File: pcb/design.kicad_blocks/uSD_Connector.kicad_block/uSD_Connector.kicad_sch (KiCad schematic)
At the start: 10 parts, among them J3 Micro_SD_Card

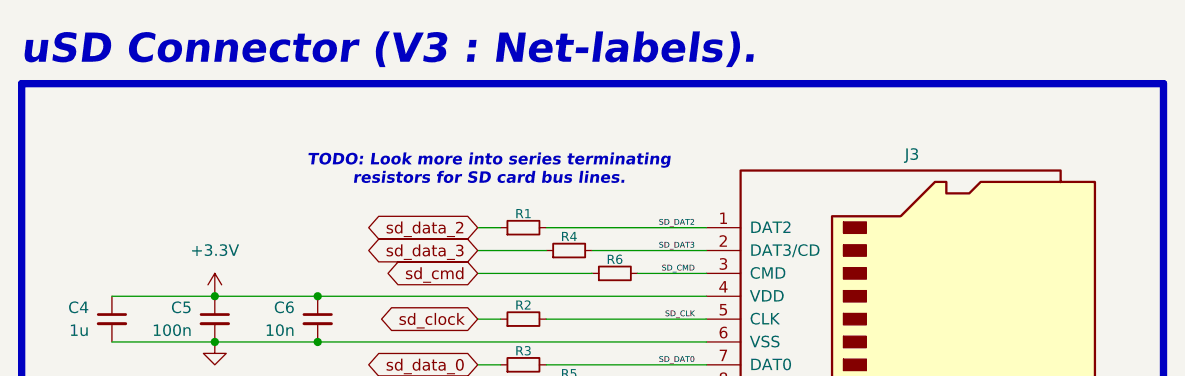
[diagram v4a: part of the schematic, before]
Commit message: Added part number to uSD connector.
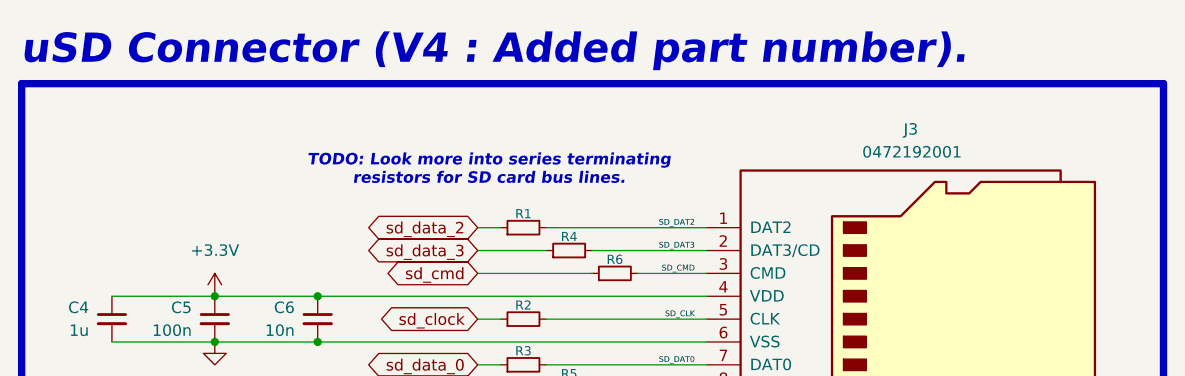
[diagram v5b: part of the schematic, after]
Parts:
- J3: value Micro_SD_Card -> 0472192001
- R1, R2, R3, R4, R5, R6: now in the parts list
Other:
- note added: "uSD Connector (V4 : Added part number)."
- note removed: "uSD Connector (V3 : Net-labels)."
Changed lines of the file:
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@@
 		)
 	)
-	(text "uSD Connector (V3 : Net-labels)."
+	(text "uSD Connector (V4 : Added part number)."
 		(exclude_from_sim no)
 		(at 340.36 165.1 0)
@@
 		(unit 1)
 		(exclude_from_sim no)
-		(in_bom no)
+		(in_bom yes)
 		(on_board yes)
 		(dnp no)
@@
 		(unit 1)
 		(exclude_from_sim no)
-		(in_bom no)
+		(in_bom yes)
 		(on_board yes)
 		(dnp no)
@@
 		(unit 1)
 		(exclude_from_sim no)
-		(in_bom no)
+		(in_bom yes)
 		(on_board yes)
 		(dnp no)
@@
 		(unit 1)
 		(exclude_from_sim no)
-		(in_bom no)
+		(in_bom yes)
 		(on_board yes)
 		(dnp no)
@@
 		(unit 1)
 		(exclude_from_sim no)
-		(in_bom no)
+		(in_bom yes)
 		(on_board yes)
 		(dnp no)
@@
 		(dnp no)
 		(property "Reference" "J3"
-			(at 439.42 174.752 0)
-			(effects
-				(font
-					(size 1.27 1.27)
-				)
-			)
-		)
-		(property "Value" "Micro_SD_Card"
-			(at 440.055 173.99 0)
-			(effects
-				(font
-					(size 1.27 1.27)
-				)
-				(hide yes)
+			(at 439.293 171.958 0)
+			(effects
+				(font
+					(size 1.27 1.27)
+				)
+			)
+		)
+		(property "Value" "0472192001"
+			(at 439.42 174.498 0)
+			(effects
+				(font
+					(size 1.27 1.27)
+				)
 			)
 		)
@@
 		(unit 1)
 		(exclude_from_sim no)
-		(in_bom no)
+		(in_bom yes)
 		(on_board yes)
 		(dnp no)

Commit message: Addressed ERC issues.
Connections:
- net SD_CLK renamed SD_CONNECTOR_CLK
- net SD_CMD renamed SD_CONNECTOR_CMD
- net SD_DAT0 renamed SD_CONNECTOR_DAT0
- net SD_DAT1 renamed SD_CONNECTOR_DAT1
- net SD_DAT2 renamed SD_CONNECTOR_DAT2
- net SD_DAT3 renamed SD_CONNECTOR_DAT3
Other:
- note added: "uSD Connector (V5 : Addressed ERC)."
- note removed: "uSD Connector (V4 : Added part number)."
- moved on the sheet: J3
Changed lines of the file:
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@@
 	(rectangle
 		(start 340.487 166.878)
-		(end 467.36 212.09)
+		(end 477.52 212.09)
 		(stroke
 			(width 0.8128)
@@
 		)
 	)
-	(text "uSD Connector (V4 : Added part number)."
+	(text "uSD Connector (V5 : Addressed ERC)."
 		(exclude_from_sim no)
 		(at 340.36 165.1 0)
@@
 	(wire
 		(pts
-			(xy 398.78 182.88) (xy 416.56 182.88)
-		)
-		(stroke
-			(width 0)
-			(type default)
-		)
-	)
-	(wire
-		(pts
-			(xy 403.86 200.66) (xy 416.56 200.66)
-		)
-		(stroke
-			(width 0)
-			(type default)
-		)
-	)
-	(wire
-		(pts
-			(xy 373.38 195.58) (xy 416.56 195.58)
-		)
-		(stroke
-			(width 0)
-			(type default)
-		)
-	)
-	(wire
-		(pts
 			(xy 361.95 195.58) (xy 350.52 195.58)
 		)
@@
 	(wire
 		(pts
-			(xy 403.86 185.42) (xy 416.56 185.42)
-		)
-		(stroke
-			(width 0)
-			(type default)
-		)
-	)
-	(wire
-		(pts
-			(xy 398.78 198.12) (xy 416.56 198.12)
+			(xy 373.38 190.5) (xy 425.45 190.5)
+		)
+		(stroke
+			(width 0)
+			(type default)
+		)
+	)
+	(wire
+		(pts
+			(xy 403.86 185.42) (xy 425.45 185.42)
 		)
 		(stroke
@@
 	(wire
 		(pts
+			(xy 408.94 187.96) (xy 425.45 187.96)
+		)
+		(stroke
+			(width 0)
+			(type default)
+		)
+	)
+	(wire
+		(pts
 			(xy 361.95 190.5) (xy 373.38 190.5)
 		)
@@
 	(wire
 		(pts
+			(xy 398.78 193.04) (xy 425.45 193.04)
+		)
+		(stroke
+			(width 0)
+			(type default)
+		)
+	)
+	(wire
+		(pts
+			(xy 403.86 200.66) (xy 425.45 200.66)
+		)
+		(stroke
+			(width 0)
+			(type default)
+		)
+	)
+	(wire
+		(pts
 			(xy 393.7 182.88) (xy 391.16 182.88)
 		)
@@
 	(wire
 		(pts
+			(xy 398.78 198.12) (xy 425.45 198.12)
+		)
+		(stroke
+			(width 0)
+			(type default)
+		)
+	)
+	(wire
+		(pts
+			(xy 373.38 195.58) (xy 425.45 195.58)
+		)
+		(stroke
+			(width 0)
+			(type default)
+		)
+	)
+	(wire
+		(pts
 			(xy 350.52 190.5) (xy 361.95 190.5)
 		)
@@
 	(wire
 		(pts
-			(xy 373.38 190.5) (xy 416.56 190.5)
-		)
-		(stroke
-			(width 0)
-			(type default)
-		)
-	)
-	(wire
-		(pts
-			(xy 398.78 193.04) (xy 416.56 193.04)
+			(xy 398.78 182.88) (xy 425.45 182.88)
 		)
 		(stroke
@@
 		)
 	)
-	(wire
-		(pts
-			(xy 408.94 187.96) (xy 416.56 187.96)
-		)
-		(stroke
-			(width 0)
-			(type default)
-		)
-	)
-	(label "SD_CMD"
-		(at 415.29 187.96 180)
+	(label "SD_CONNECTOR_CMD"
+		(at 424.18 187.96 180)
 		(effects
 			(font
@@
 		)
 	)
-	(label "SD_CLK"
-		(at 415.29 193.04 180)
+	(label "SD_CONNECTOR_CLK"
+		(at 424.18 193.04 180)
 		(effects
 			(font
@@
 		)
 	)
-	(label "SD_DAT0"
-		(at 415.29 198.12 180)
+	(label "SD_CONNECTOR_DAT0"
+		(at 424.18 198.12 180)
 		(effects
 			(font
@@
 		)
 	)
-	(label "SD_DAT3"
-		(at 415.29 185.42 180)
+	(label "SD_CONNECTOR_DAT3"
+		(at 424.18 185.42 180)
 		(effects
 			(font
@@
 		)
 	)
-	(label "SD_DAT2"
-		(at 415.29 182.88 180)
+	(label "SD_CONNECTOR_DAT2"
+		(at 424.18 182.88 180)
 		(effects
 			(font
@@
 		)
 	)
-	(label "SD_DAT1"
-		(at 415.29 200.66 180)
+	(label "SD_CONNECTOR_DAT1"
+		(at 424.18 200.66 180)
 		(effects
 			(font
@@
 	(symbol
 		(lib_id "Connector:Micro_SD_Card")
-		(at 439.42 190.5 0)
+		(at 448.31 190.5 0)
 		(unit 1)
 		(exclude_from_sim no)
@@
 		(dnp no)
 		(property "Reference" "J3"
-			(at 439.293 171.958 0)
+			(at 448.183 171.958 0)
 			(effects
 				(font
@@
 		)
 		(property "Value" "0472192001"
-			(at 439.42 174.498 0)
+			(at 448.31 174.498 0)
 			(effects
 				(font
@@
 		)
 		(property "Footprint" "pcb:microSD_HC_Molex_47219-2001"
-			(at 468.63 182.88 0)
+			(at 477.52 182.88 0)
 			(effects
 				(font
@@
 		)
 		(property "Datasheet" "https://www.we-online.com/components/products/datasheet/693072010801.pdf"
-			(at 439.42 190.5 0)
+			(at 448.31 190.5 0)
 			(effects
 				(font
@@
 		)
 		(property "Description" "Micro SD Card Socket"
-			(at 439.42 190.5 0)
+			(at 448.31 190.5 0)
 			(effects
 				(font
@@
 	(symbol
 		(lib_id "power:GND")
-		(at 459.74 205.74 90)
+		(at 468.63 205.74 90)
 		(unit 1)
 		(exclude_from_sim no)
@@
 		(fields_autoplaced yes)
 		(property "Reference" "#PWR026"
-			(at 466.09 205.74 0)
+			(at 474.98 205.74 0)
 			(effects
 				(font
@@
 		)
 		(property "Value" "GND"
-			(at 463.55 205.7399 90)
+			(at 472.44 205.7399 90)
 			(effects
 				(font
@@
 		)
 		(property "Footprint" ""
-			(at 459.74 205.74 0)
+			(at 468.63 205.74 0)
 			(effects
 				(font
@@
 		)
 		(property "Datasheet" ""
-			(at 459.74 205.74 0)
+			(at 468.63 205.74 0)
 			(effects
 				(font
@@
 		)
 		(property "Description" "Power symbol creates a global label with name \"GND\" , ground"
-			(at 459.74 205.74 0)
-			(effects
-				(font
+			(at 468.63 205.74 0)
+			(effects
+				(font

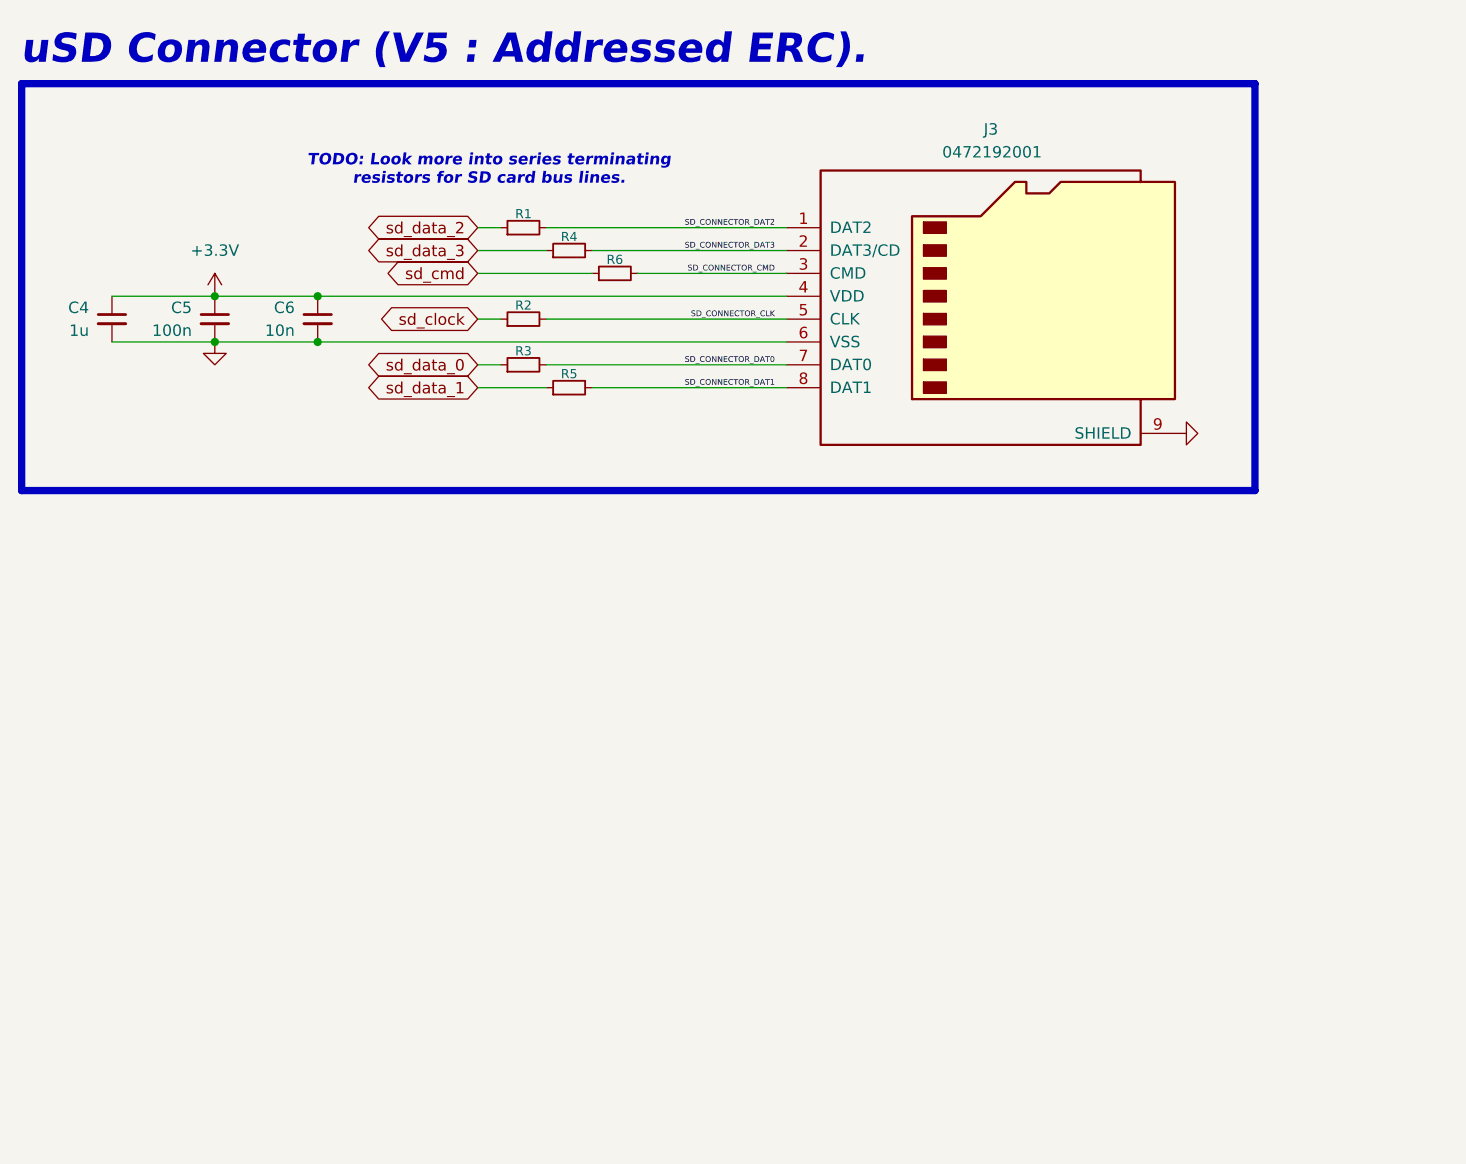
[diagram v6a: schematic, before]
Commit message: uSD Connector (V6 : Hierarchical labels).
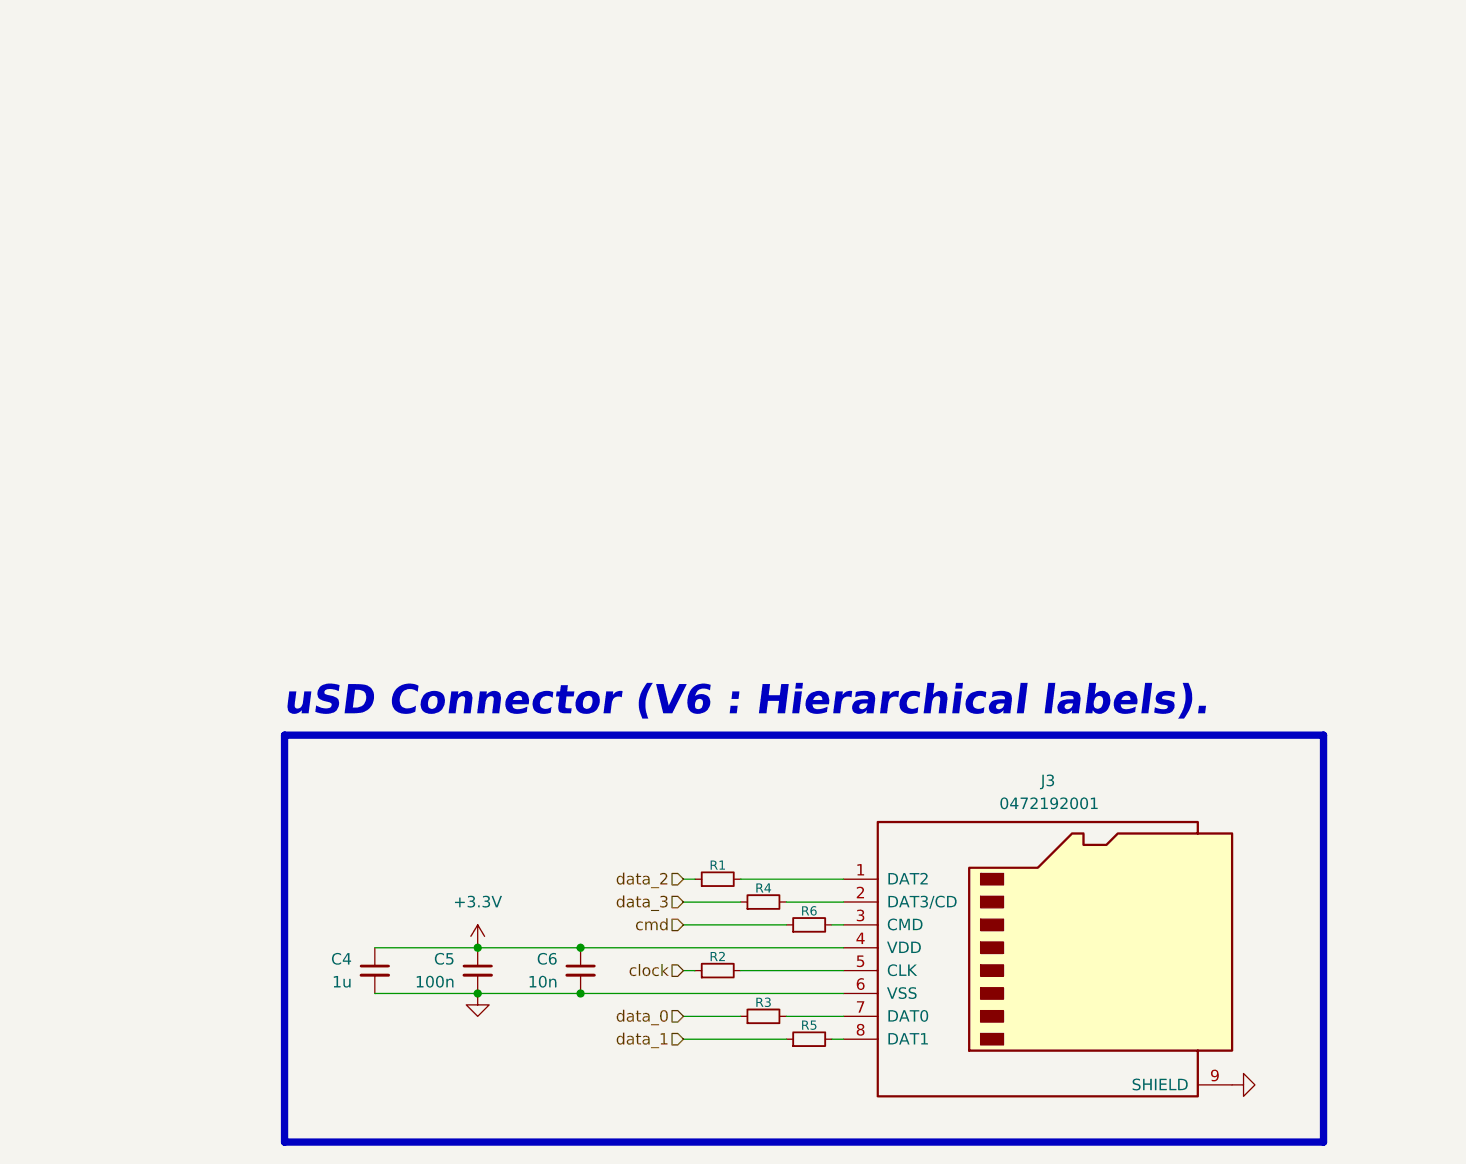
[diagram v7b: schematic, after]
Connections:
- net SD_CONNECTOR_CLK: no longer names the net of J3.5 (CLK), R2.2
- net SD_CONNECTOR_CMD: no longer names the net of J3.3 (CMD), R6.2
- net SD_CONNECTOR_DAT0: no longer names the net of J3.7 (DAT0), R3.2
- net SD_CONNECTOR_DAT1: no longer names the net of J3.8 (DAT1), R5.2
- net SD_CONNECTOR_DAT2: no longer names the net of J3.1 (DAT2), R1.2
- net SD_CONNECTOR_DAT3: no longer names the net of J3.2 (DAT3/CD), R4.2
- net sd_clock renamed clock
- net sd_cmd renamed cmd
- net sd_data_0 renamed data_0
- net sd_data_1 renamed data_1
- net sd_data_2 renamed data_2
- net sd_data_3 renamed data_3
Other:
- note added: "uSD Connector (V6 : Hierarchical labels)."
- note removed: "TODO: Look more into series terminating resistors for SD card bus lines."
- note removed: "uSD Connector (V5 : Addressed ERC)."
- moved on the sheet: C4, C5, C6, J3, R1, R2, R3, R4, R5, R6

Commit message: Removed series resistors for `uSD Connector` design block.
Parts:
- removed R1, R2, R3, R4, R5, R6: R_Small, Resistor_SMD:R_1206_3216Metric_Pad1.30x1.75mm_HandSolder, symbol Device:R_Small
- renumbered C4 to C24, C5 to C25, C6 to C26
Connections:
- net clock: now also J3.5 (CLK)
- net cmd: now also J3.3 (CMD)
- net data_0: now also J3.7 (DAT0)
- net data_1: now also J3.8 (DAT1)
- net data_2: now also J3.1 (DAT2)
- net data_3: now also J3.2 (DAT3/CD)
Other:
- note added: "uSD Connector (V7 : Removed series resistor)."
- note removed: "uSD Connector (V6 : Hierarchical labels)."
- moved on the sheet: C24, C25, C26, J3
